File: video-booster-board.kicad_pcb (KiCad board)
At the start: 4 copper layers, 36.5 x 41.5 mm, 105 parts, among them J1 0473460001, J10 61300411121, J2 HDMI-PE10-19-LF, J3 HDMI-PE10-19-LF, J4 M20-9990246, J5 M20-9990246, J6 685119134923_, J7 M20-9990246, J8 M20-9990246, J9 685119134923_, Q1 BSS138-7-F, Q2 BSS138-7-F, U1 PTN3363, U2 EFM32HG309, U3 PTN3363, U4 LP2985-33DBVR

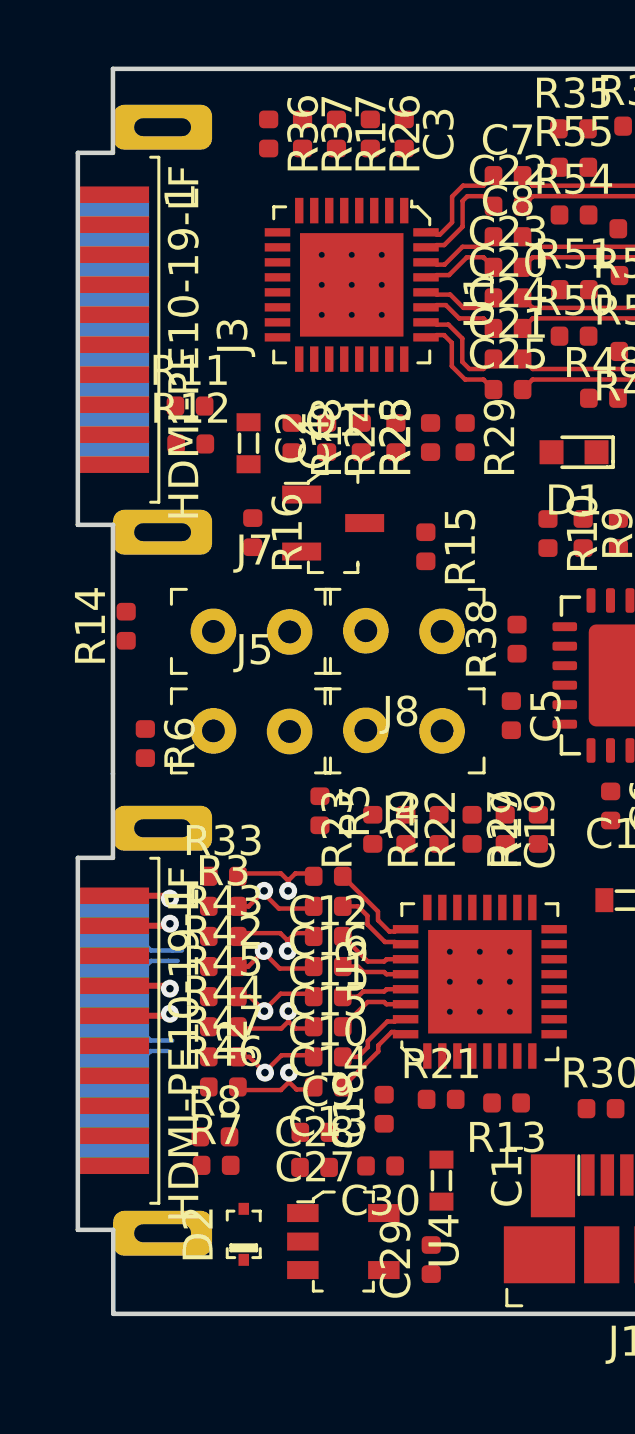
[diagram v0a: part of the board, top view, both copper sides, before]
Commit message: Updated footprints with new 3D models
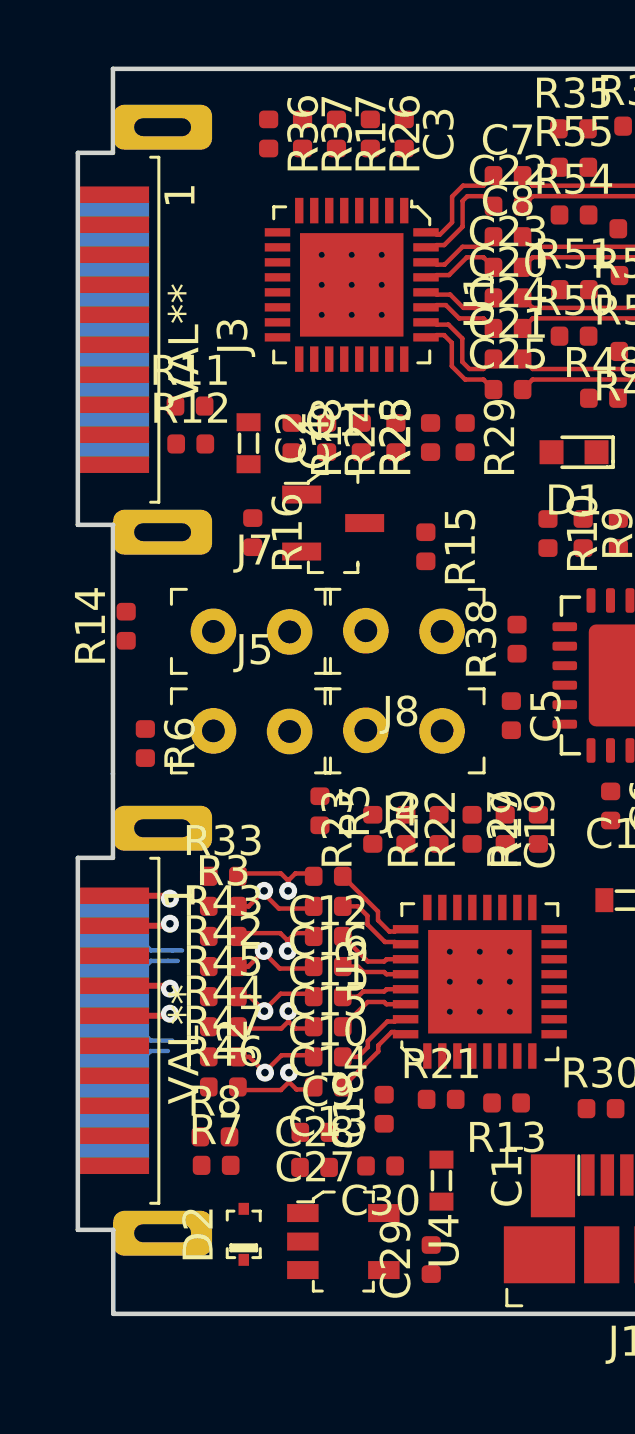
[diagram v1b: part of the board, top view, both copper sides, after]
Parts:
- J2, J3: value HDMI-PE10-19-LF -> VAL**

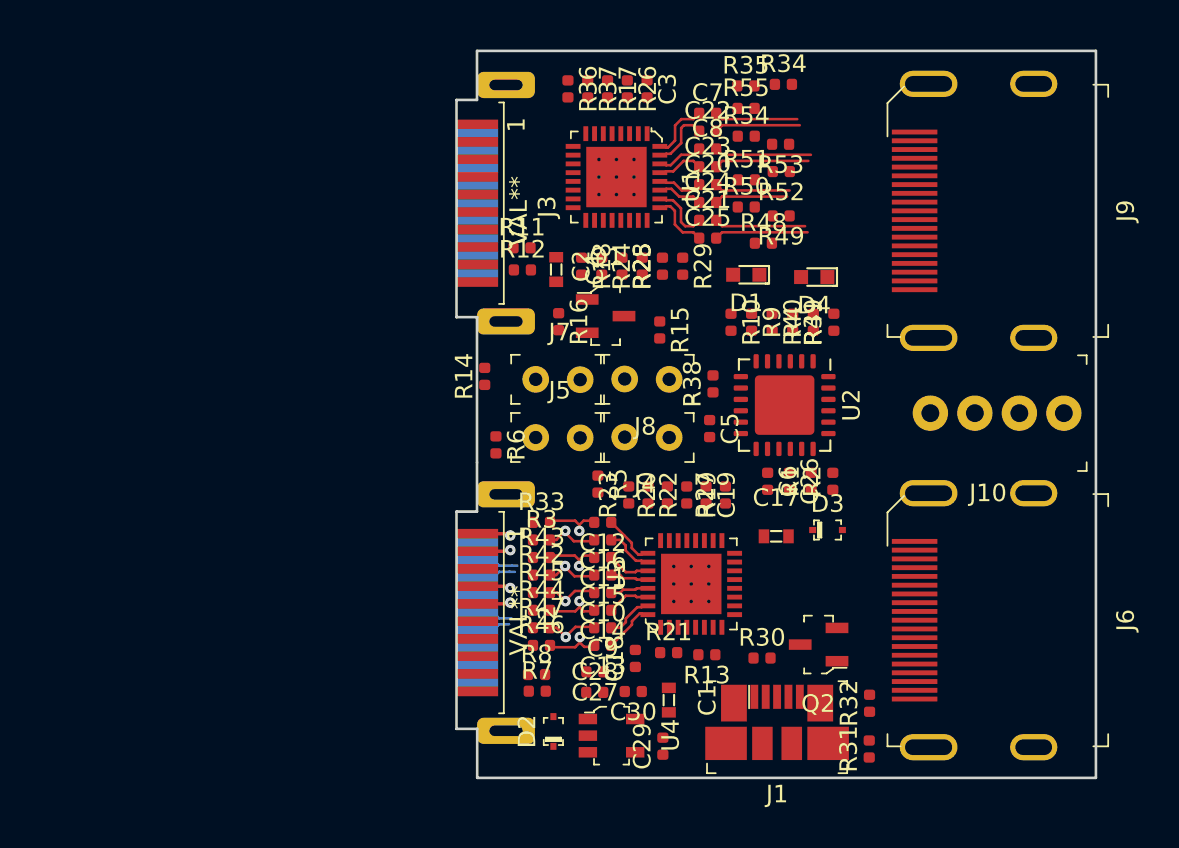
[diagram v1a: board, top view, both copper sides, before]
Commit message: Initial placement of new components. Diff lanes routed
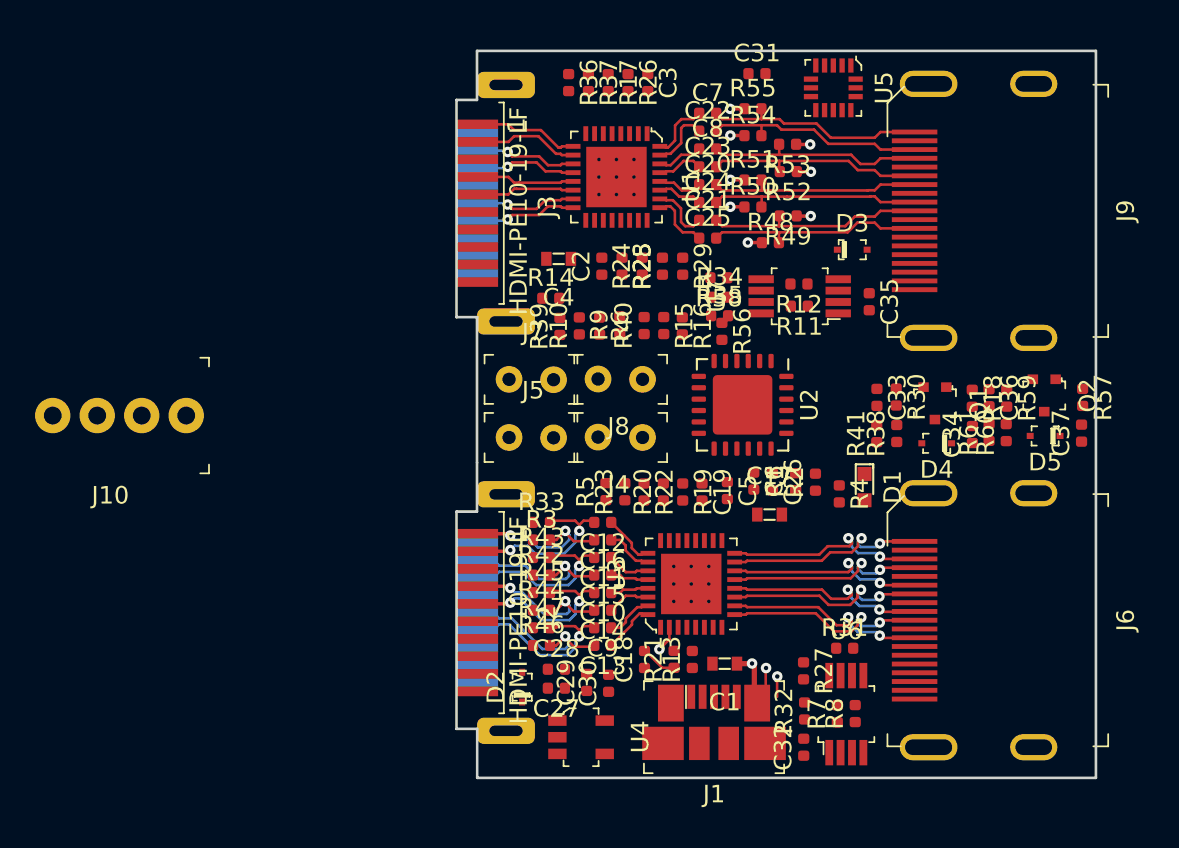
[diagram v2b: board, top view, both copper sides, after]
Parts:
- added C31: C_100n_0402_6V3, antmicro-footprints:0402-cap, F.Cu at (130.7, 59.8)
- added C32: C_100n_0402_6V3, antmicro-footprints:0402-cap, F.Cu at (133.3, 98.2)
- added C33: C_220p_0402, antmicro-footprints:0402-cap, F.Cu at (137.5, 78.3)
- added C34: C_220p_0402, antmicro-footprints:0402-cap, F.Cu at (142.9, 80.4)
- added C35: C_100n_0402_6V3, antmicro-footprints:0402-cap, F.Cu at (137.1, 72.8)
- added C36: C_220p_0402, antmicro-footprints:0402-cap, F.Cu at (143.9, 78.3)
- added C37: C_220p_0402, antmicro-footprints:0402-cap, F.Cu at (149.2, 80.3)
- added D5: 1N4148X-TP, antmicro-footprints:SOD-523, F.Cu at (147.1, 80.5)
- added R56: R_18k_0402, antmicro-footprints:0402-res, F.Cu at (128.7, 74.5)
- added R57: R_100k_0402, antmicro-footprints:0402-res, F.Cu at (149.2, 78.3)
- added R58: R_100k_0402, antmicro-footprints:0402-res, F.Cu at (128.5, 71.5)
- added R59: R_47k_0402, antmicro-footprints:0402-res, F.Cu at (144.9, 78.3)
- added R60: R_27k_0402, antmicro-footprints:0402-res, F.Cu at (144.9, 80.3)
- added R61: R_220R_0402, antmicro-footprints:0402-res, F.Cu at (143.9, 80.3)
- added U5: PCA9554BS3, antmicro-footprints:VQFN-16_3x3mm, F.Cu at (135.0, 60.6)
- added U6: PCA9517ADP, antmicro-footprints:TSSOP-8_W3mm, F.Cu at (135.8, 96.4)
- added U7: PCA9517ADP, antmicro-footprints:TSSOP-8_W3mm, F.Cu at (133.1, 72.5)
- D4: value LG_L29K-G2J1-24-Z -> 1N4148X-TP; footprint antmicro-footprints:LED_0603 -> antmicro-footprints:SOD-523
- J2, J3: value VAL** -> HDMI-PE10-19-LF
- Q1, Q2: value BSS138-7-F -> BC817W; footprint antmicro-footprints:SOT-23-3 -> antmicro-footprints:SOT-323
- R16: value R_10k_0402 -> R_18k_0402
- R18, R27: value R_10k_0402 -> R_100k_0402
- R30: value R_10k_0402 -> R_47k_0402
- R38: value R_10k_0402 -> R_27k_0402
- R41: value R_330R_0402 -> R_220R_0402
- moved J10 50.1 mm to (98.1, 79.3)
- moved R18 23.5 mm to (142.9, 78.3)
- moved Q1 19.4 mm to (140.8, 78.6), turned to 270 degrees
- moved Q2 19.2 mm to (147.1, 78.2), turned to 270 degrees
- moved R8 18.3 mm to (136.3, 96.3), turned to 90 degrees
- moved R7 17.2 mm to (135.2, 96.3), turned to 90 degrees
- moved R30 16.8 mm to (138.6, 78.3), turned to 270 degrees
- moved R11 16.2 mm to (133.1, 73.1), turned to 180 degrees
- moved D3 16.1 mm to (136.1, 69.8)
- moved R12 15.8 mm to (133.0, 71.8), turned to 180 degrees
- moved D1 13.9 mm to (136.8, 83.4), turned to 270 degrees
- moved R39 13.3 mm to (119.4, 74.2), turned to 90 degrees
- moved R35 13.2 mm to (128.5, 73.6)
- moved R34 12.7 mm to (128.5, 72.6)
- moved D4 11.8 mm to (140.9, 80.9)
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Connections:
- J2 pad 15: Net-(J2-Pad15) -> /SRC_TX_SCL
- J2 pad 16: Net-(J2-Pad16) -> /SRC_TX_SDA
- J3 pad 15: Net-(J3-Pad15) -> /RX_SCL
- J3 pad 16: Net-(J3-Pad16) -> /RX_SDA
- J9 pad 15: /RX_SCL -> /SRC_RX_SCL
- J9 pad 16: /RX_SDA -> /SRC_RX_SDA
- Q1 pad 1: /RX_5V -> Net-(C34-Pad2)
- Q1 pad 2: GND -> Net-(Q1-Pad2)
- Q1 pad 3: Net-(Q1-Pad3) -> /TX_CEC
- Q2 pad 1: /TX_5V -> Net-(C37-Pad2)
- Q2 pad 2: GND -> Net-(Q2-Pad2)
- Q2 pad 3: Net-(Q2-Pad3) -> /RX_CEC
- R10 pad 2: Net-(R10-Pad2) -> /TX_EQ1_R
- R11 pad 1: Net-(J3-Pad15) -> /SRC_RX_SCL
- R11 pad 2: /RX_SDA -> /RX_SCL
- R12 pad 1: Net-(J3-Pad16) -> /SRC_RX_SDA
- R12 pad 2: /RX_SCL -> /RX_SDA
- R16 pad 1: GND -> VDD
- R16 pad 2: /RX_5V -> /TX_CEC_OUT
- R18 pad 1: Net-(Q1-Pad3) -> /TX_CEC_OUT
- R18 pad 2: VDD -> Net-(C34-Pad2)
- R27 pad 1: Net-(Q2-Pad3) -> /TX_I2C_PASS
- R27 pad 2: VDD -> /TX_5V
- R30 pad 1: GND -> /TX_CEC_IN
- R30 pad 2: /TX_5V -> Net-(D4-PadA)
- R38 pad 1: /TX_DCC_EN -> VDD
- R38 pad 2: Net-(R38-Pad2) -> Net-(D4-PadA)
- R39 pad 2: Net-(R39-Pad2) -> /RX_EQ0_R
- R40 pad 2: Net-(R40-Pad2) -> /RX_EQ1_R
- R41 pad 1: Net-(R41-Pad1) -> Net-(Q1-Pad2)
- R41 pad 2: Net-(D4-Pad1) -> GND
- R7 pad 1: Net-(J2-Pad15) -> /SRC_TX_SCL
- R7 pad 2: /TX_SDA -> /TX_SCL
- R8 pad 1: Net-(J2-Pad16) -> /SRC_TX_SDA
- R8 pad 2: /TX_SCL -> /TX_SDA
- R9 pad 2: Net-(R9-Pad2) -> /TX_EQ0_R
- U1 pad 17: Net-(Q1-Pad3) -> GND
- U1 pad 19: /RX_SDA -> /SRC_RX_SCL
- U1 pad 20: /RX_SCL -> /SRC_RX_SDA
- U1 pad 21: Net-(U1-Pad21) -> /RX_HPD
- U1 pad 5: Net-(U1-Pad5) -> /MCU_RX_HPD
- U2 pad 1: Net-(R4-Pad1) -> /MCU_RX_HPD
- U2 pad 10: /TX_HIZ_EN -> /TX_DCC_EN
- U2 pad 11: /RX_HIZ_EN -> /MCU_TX_HPD
- U2 pad 21: Net-(R41-Pad1) -> Net-(R4-Pad1)
- U2 pad 3: Net-(R39-Pad2) -> /RX_CEC_OUT
- U2 pad 4: Net-(R40-Pad2) -> /TX_CEC_OUT
- U2 pad 5: Net-(R9-Pad2) -> /TX_CEC_IN
- U2 pad 6: Net-(R10-Pad2) -> /RX_CEC_IN
- U2 pad 8: Net-(R38-Pad2) -> /RX_DCC_EN
- U3 pad 17: Net-(Q2-Pad3) -> GND
- U3 pad 19: /TX_SDA -> /SRC_TX_SCL
- U3 pad 20: /TX_SCl -> /SRC_TX_SDA
- U3 pad 21: Net-(U3-Pad21) -> /TX_HPD
- U3 pad 5: Net-(U3-Pad5) -> /MCU_TX_HPD
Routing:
- net /TX_OUT_CLK_N: track 0.00 -> 12.0 mm, vias 0 -> 2
- net /TX_OUT_CLK_P: track 0.00 -> 12.0 mm, vias 0 -> 2
- net /TX_OUT_D0_N: track 0.00 -> 11.8 mm, vias 0 -> 2
- net /TX_OUT_D0_P: track 0.00 -> 11.8 mm, vias 0 -> 2
- net /TX_OUT_D2_N: track 0.00 -> 11.8 mm, vias 0 -> 2
- net /TX_OUT_D2_P: track 0.00 -> 11.8 mm, vias 0 -> 2
- net /TX_OUT_D1_N: track 0.00 -> 11.7 mm, vias 0 -> 2
- net /TX_OUT_D1_P: track 0.00 -> 11.7 mm, vias 0 -> 2
- net VDD: track 0.00 -> 8.56 mm, vias 0 -> 8
- net /RX_IN_D0_N: track 4.18 -> 12.2 mm
- net /RX_IN_D2_P: track 4.76 -> 12.7 mm
- net /RX_IN_D0_P: track 4.33 -> 12.2 mm
- net /RX_IN_D2_N: track 4.91 -> 12.7 mm
- net /RX_IN_CLK_P: track 5.21 -> 12.4 mm
- net /RX_IN_CLK_N: track 5.36 -> 12.4 mm
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
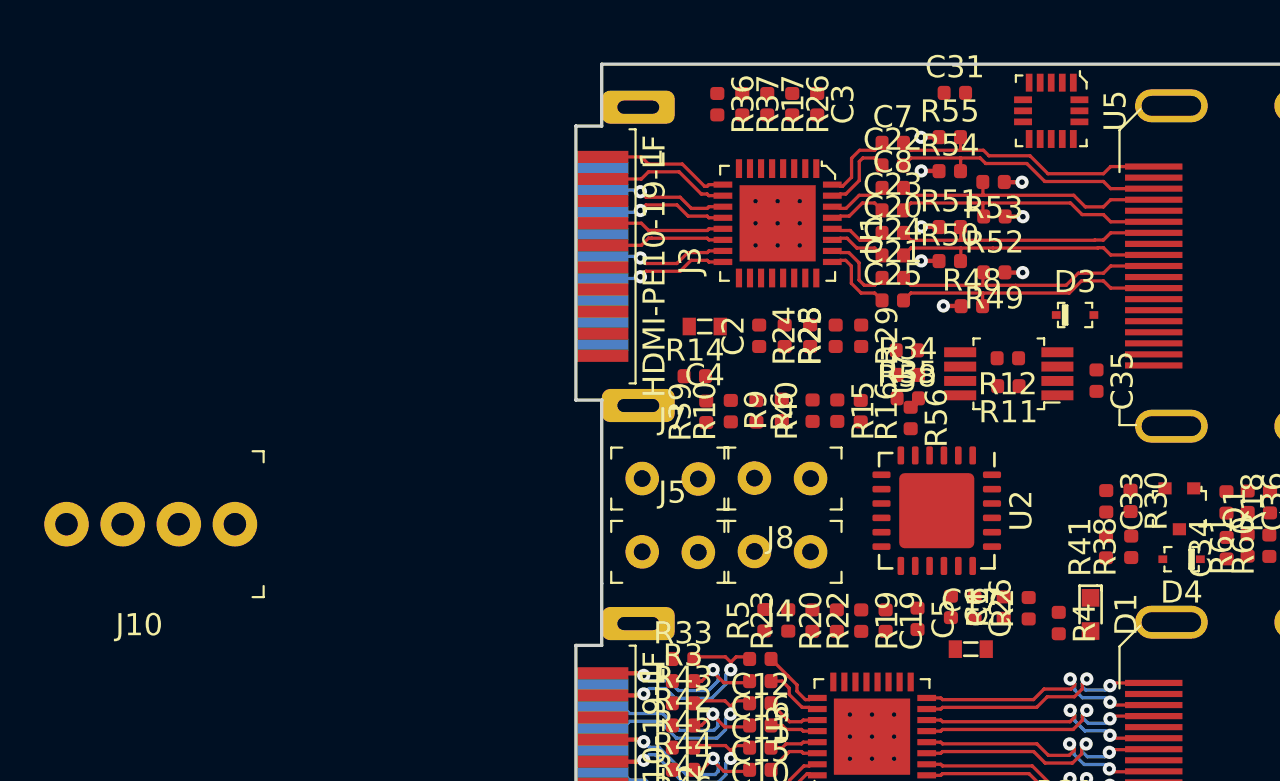
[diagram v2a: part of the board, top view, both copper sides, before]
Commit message: Key features description added. Programming connector changed to smaller
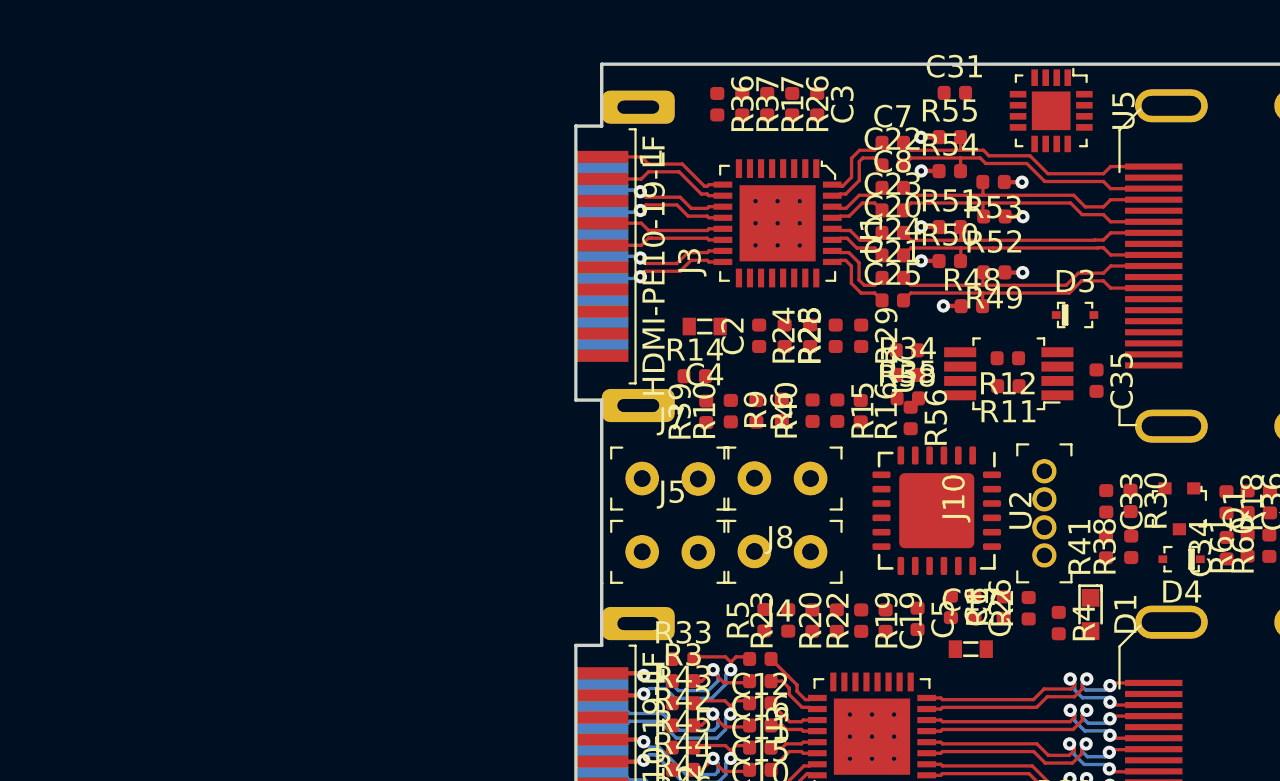
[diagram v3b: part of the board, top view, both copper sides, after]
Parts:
- J10: value 61300411121 -> MC-HVT1-S04-G; footprint antmicro-footprints:PinHeader_1x4_P2.54mm_Drill1.02mm -> antmicro-footprints:PinHeader_1x4_P1.27mm_Drill.7mm
- U5: footprint antmicro-footprints:VQFN-16_3x3mm -> antmicro-footprints:VFQFN-16-1EP_3x3mm
- moved J10 36.7 mm to (134.7, 80.7), turned to 90 degrees
